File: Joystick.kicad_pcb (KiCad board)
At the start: 2 copper layers, 2 parts, among them J1 Conn_02x08_Counter_Clockwise, J2 DE9_Male_MountingHoles

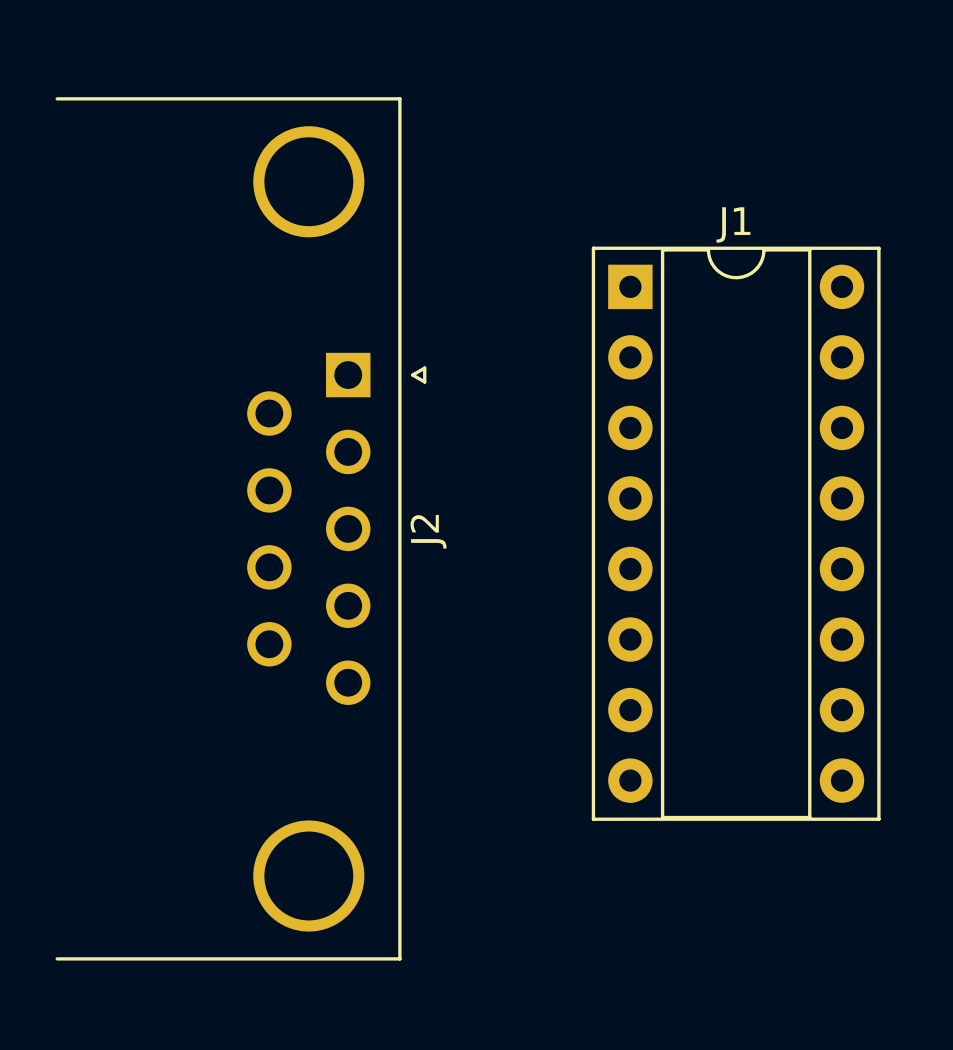
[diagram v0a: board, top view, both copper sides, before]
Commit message: Draw tracks and zones.
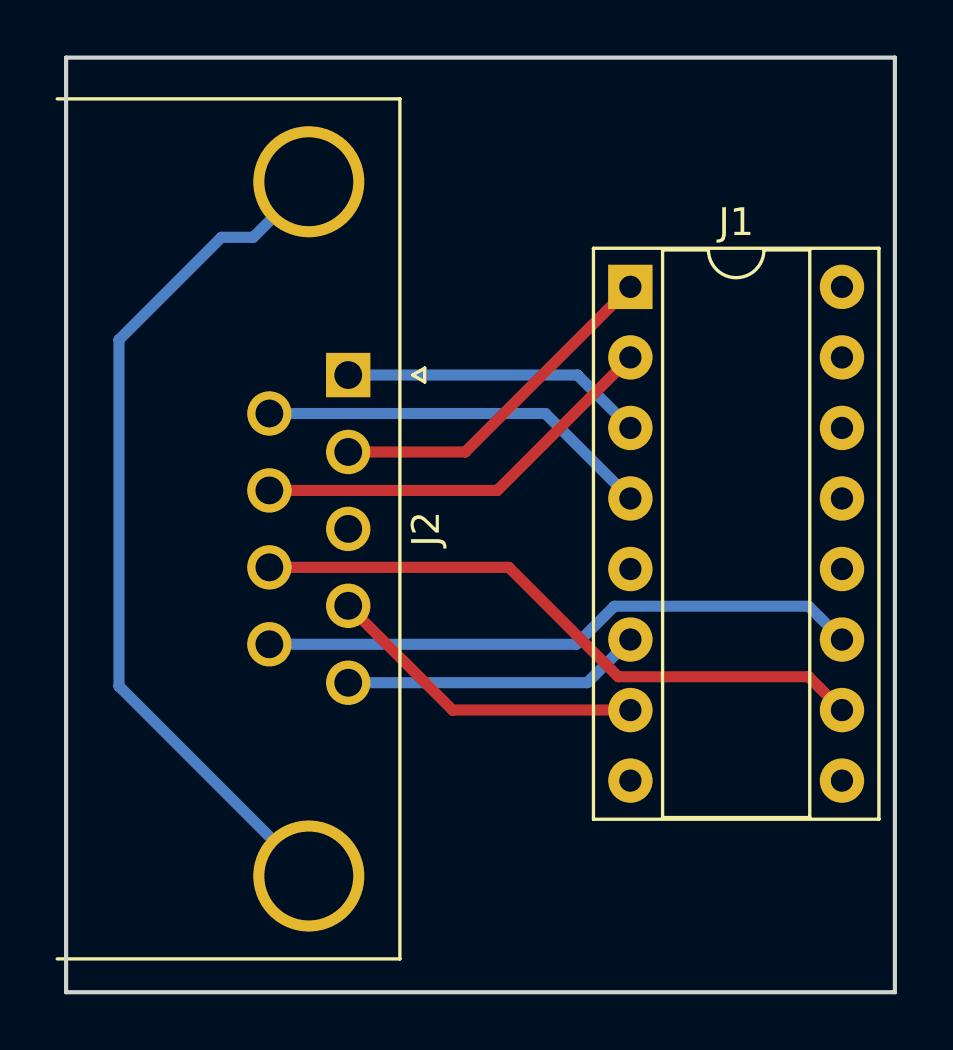
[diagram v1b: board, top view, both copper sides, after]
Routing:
- net Net-(J2-Pad0): track 0.00 -> 31.3 mm
- net /PDL1: track 0.00 -> 22.7 mm
- net /PDL3: track 0.00 -> 21.7 mm
- net /PB0: track 0.00 -> 15.0 mm
- net /PB2: track 0.00 -> 14.3 mm
- net +5V: track 0.00 -> 12.6 mm
- net /PDL2: track 0.00 -> 11.7 mm
- net /PB1: track 0.00 -> 10.9 mm
- net /PDL0: track 0.00 -> 10.8 mm
- added copper zone on B.Cu, net GND
- added copper zone on F.Cu, net GND
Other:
- board outline added: 29.8 x 33.7 mm
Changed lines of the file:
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@@
   (general
     (links 10)
-    (no_connects 10)
+    (no_connects 0)
     (area 0 0 0 0)
     (thickness 1.6)
-    (drawings 0)
-    (tracks 0)
+    (drawings 4)
+    (tracks 27)
     (zones 0)
     (modules 2)
@@
   )
   (setup
-    (last_trace_width 0.25)
+    (last_trace_width 0.4)
     (user_trace_width 0.4)
     (trace_clearance 0.2)
-    (zone_clearance 0.508)
+    (zone_clearance 0.3048)
     (zone_45_only no)
     (trace_min 0.2)
@@
     (pad_to_mask_clearance 0)
     (aux_axis_origin 0 0)
-    (visible_elements FFFFFF7F)
+    (visible_elements FFFFEF7F)
     (pcbplotparams
       (layerselection 0x00030_80000001)
@@
     )
   )
+  (gr_line (start 159.385 96.52) (end 129.54 96.52) (angle 90) (layer Edge.Cuts) (width 0.15))
+  (gr_line (start 159.385 130.175) (end 159.385 96.52) (angle 90) (layer Edge.Cuts) (width 0.15))
+  (gr_line (start 129.54 130.175) (end 159.385 130.175) (angle 90) (layer Edge.Cuts) (width 0.15))
+  (gr_line (start 129.54 96.52) (end 129.54 130.175) (angle 90) (layer Edge.Cuts) (width 0.15))
+  (segment (start 139.7 110.72) (end 143.915 110.72) (width 0.4) (layer F.Cu) (net 1))
+  (segment (start 143.915 110.72) (end 149.86 104.775) (width 0.4) (layer F.Cu) (net 1))
+  (segment (start 136.86 112.105) (end 145.07 112.105) (width 0.4) (layer F.Cu) (net 2))
+  (segment (start 145.07 112.105) (end 149.86 107.315) (width 0.4) (layer F.Cu) (net 2))
+  (segment (start 136.86 114.875) (end 145.483998 114.875) (width 0.4) (layer F.Cu) (net 3))
+  (segment (start 145.483998 114.875) (end 149.423997 118.814999) (width 0.4) (layer F.Cu) (net 3))
+  (segment (start 149.423997 118.814999) (end 156.279999 118.814999) (width 0.4) (layer F.Cu) (net 3))
+  (segment (start 156.279999 118.814999) (end 156.680001 119.215001) (width 0.4) (layer F.Cu) (net 3))
+  (segment (start 156.680001 119.215001) (end 157.48 120.015) (width 0.4) (layer F.Cu) (net 3))
+  (segment (start 139.7 107.95) (end 147.955 107.95) (width 0.4) (layer B.Cu) (net 4))
+  (segment (start 147.955 107.95) (end 149.86 109.855) (width 0.4) (layer B.Cu) (net 4))
+  (segment (start 136.86 117.645) (end 147.913998 117.645) (width 0.4) (layer B.Cu) (net 5))
+  (segment (start 147.913998 117.645) (end 149.283999 116.274999) (width 0.4) (layer B.Cu) (net 5))
+  (segment (start 149.283999 116.274999) (end 156.279999 116.274999) (width 0.4) (layer B.Cu) (net 5))
+  (segment (start 156.680001 116.675001) (end 157.48 117.475) (width 0.4) (layer B.Cu) (net 5))
+  (segment (start 156.279999 116.274999) (end 156.680001 116.675001) (width 0.4) (layer B.Cu) (net 5))
+  (segment (start 136.86 109.335) (end 146.8 109.335) (width 0.4) (layer B.Cu) (net 6))
+  (segment (start 146.8 109.335) (end 149.86 112.395) (width 0.4) (layer B.Cu) (net 6))
+  (segment (start 139.7 119.03) (end 148.305 119.03) (width 0.4) (layer B.Cu) (net 7))
+  (segment (start 148.305 119.03) (end 149.86 117.475) (width 0.4) (layer B.Cu) (net 7))
+  (segment (start 139.7 116.26) (end 143.455 120.015) (width 0.4) (layer F.Cu) (net 8))
+  (segment (start 143.455 120.015) (end 149.86 120.015) (width 0.4) (layer F.Cu) (net 8))
+  (segment (start 131.445 106.68) (end 131.445 119.155) (width 0.4) (layer B.Cu) (net 10))
+  (segment (start 131.445 119.155) (end 138.28 125.99) (width 0.4) (layer B.Cu) (net 10))
+  (segment (start 135.135001 102.989999) (end 131.445 106.68) (width 0.4) (layer B.Cu) (net 10))
+  (segment (start 138.28 100.99) (end 136.280001 102.989999) (width 0.4) (layer B.Cu) (net 10))
+  (segment (start 136.280001 102.989999) (end 135.135001 102.989999) (width 0.4) (layer B.Cu) (net 10))
+  (zone (net 9) (net_name GND) (layer B.Cu) (hatch edge 0.508)
+    (connect_pads (clearance 0.3048))
+    (min_thickness 0.254)
+    (fill yes (arc_segments 16) (thermal_gap 0.508) (thermal_bridge_width 0.508))
+    (polygon
+      (pts
+        (xy 159.385 130.175) (xy 129.54 130.175) (xy 129.54 96.52) (xy 159.385 96.52)
+      )
+    )
+  )
+  (zone (net 9) (net_name GND) (layer F.Cu) (hatch edge 0.508)
+    (connect_pads (clearance 0.3048))
+    (min_thickness 0.254)
+    (fill yes (arc_segments 16) (thermal_gap 0.508) (thermal_bridge_width 0.508))
+    (polygon
+      (pts
+        (xy 159.385 130.175) (xy 129.54 130.175) (xy 129.54 96.52) (xy 159.385 96.52)
+      )
+    )
+  )

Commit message: Add text on silkscreen.
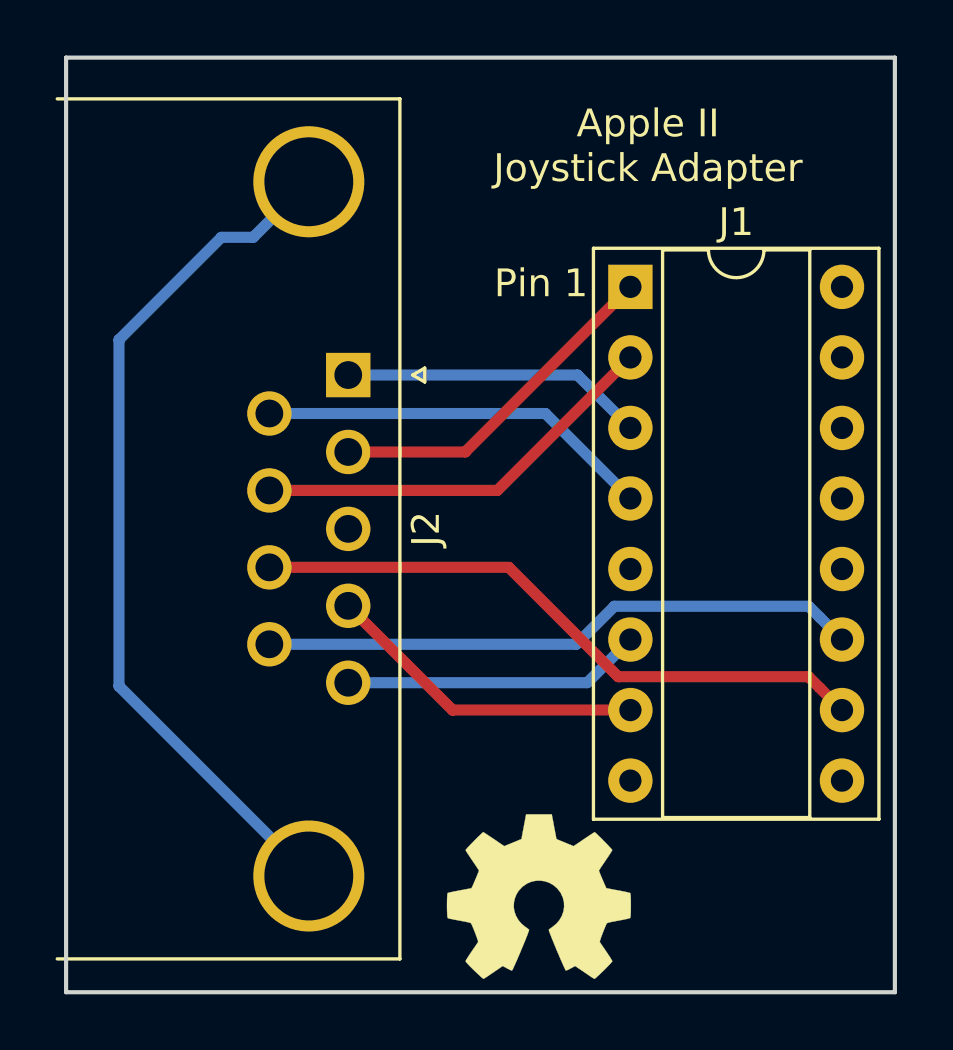
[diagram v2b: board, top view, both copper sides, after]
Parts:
- added REF***: OSHW-Symbol_6.7x6mm_SilkScreen, Symbols:OSHW-Symbol_6.7x6mm_SilkScreen, F.Cu at (146.6, 126.7)
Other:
- board text added: "Apple II Joystick Adapter"
- board text added: "Patrick Pelletier 2018-09-05"
- board text added: "Pin 1"
- board text added: "https://github.com/ppelleti/A2JoystickAdapter"
